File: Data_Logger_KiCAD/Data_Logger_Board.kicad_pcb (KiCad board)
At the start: 6 copper layers, 45.1 x 63.7 mm, 98 parts, among them J1 USB_C_Receptacle_USB2.0_16P, J2 Screw_Terminal_01x02, J3 Micro_SD_Card, Q1 Q_NMOS_GSD, SW1 SW_Push, SW2 SW_Push, U1 LSM6DSO32TR, U10 BMP390L, U11 MMC5983MA, U12 AMS1117-3.3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

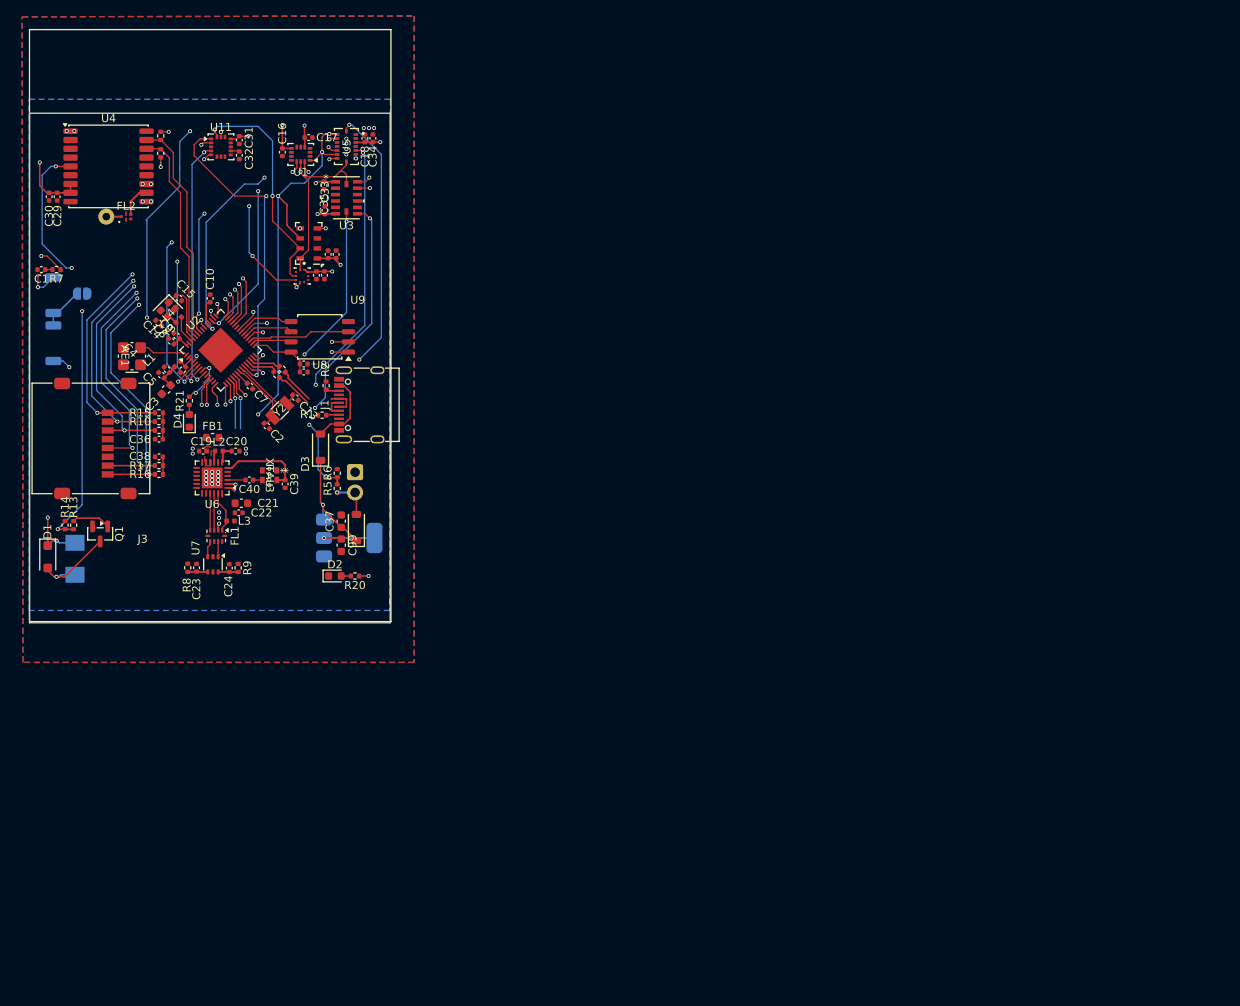
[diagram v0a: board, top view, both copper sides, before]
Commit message: Updates to board routing
Added SMA connector for radio, added additional SPI routing. Reworked some routing for other modules.
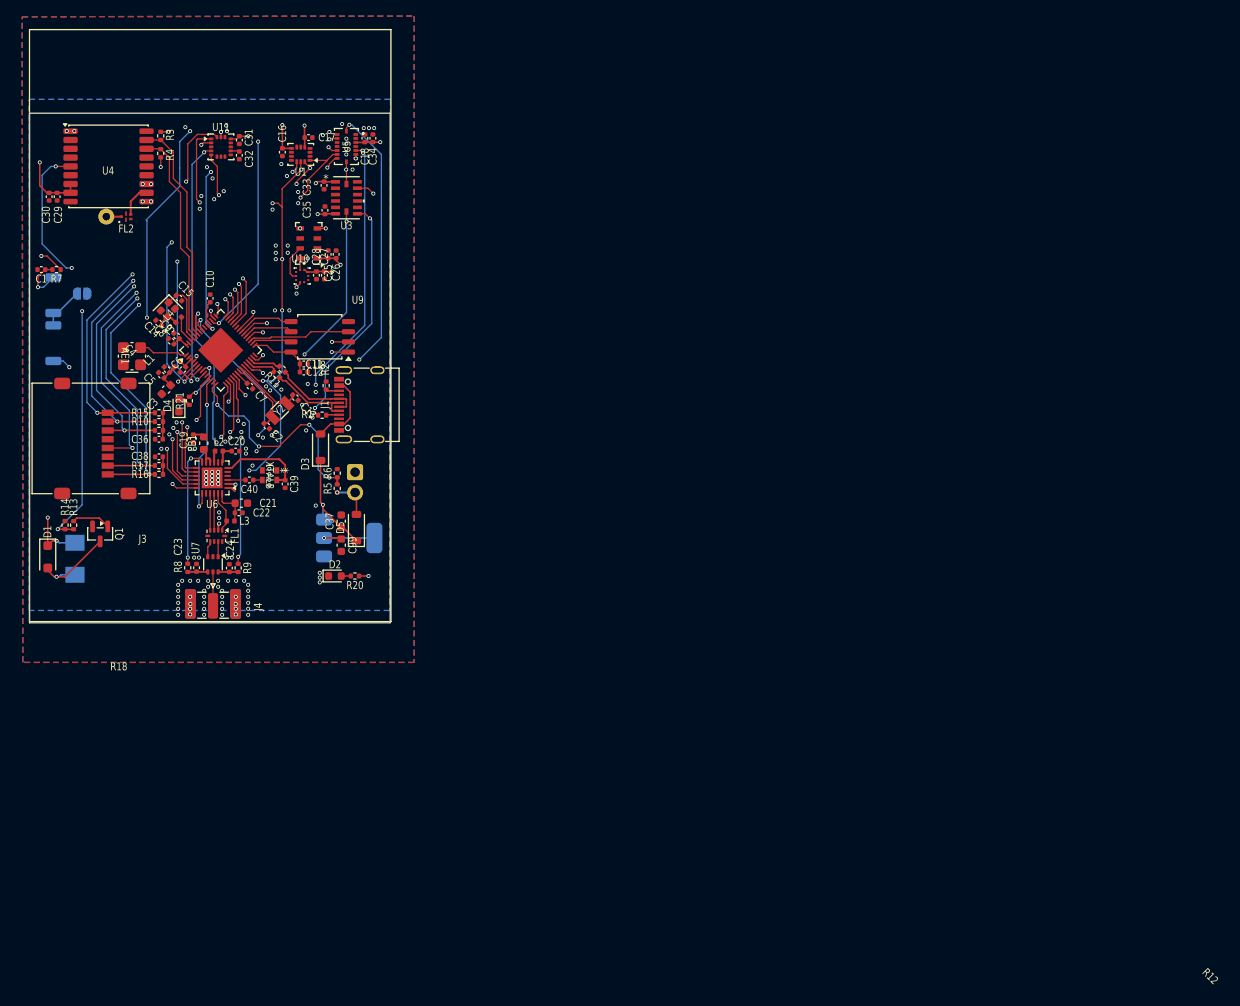
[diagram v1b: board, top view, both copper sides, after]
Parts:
- added J4: Conn_Coaxial_Small, Connector_Coaxial:SMA_Samtec_SMA-J-P-H-ST-EM1_EdgeMount, F.Cu at (142.9, 108.1)
- moved D4 2.30 mm to (138.6, 83.1)
- moved C19 2.00 mm to (140.4, 87.2), turned to -90 degrees
- moved FB1 1.31 mm to (141.7, 87.8), turned to 90 degrees
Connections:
- U7 pad 5: /MCU/radio/SMA_CONN -> /MCU/SMA_CONN
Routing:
- net /MCU/MISO: track 108.9 -> 57.8 mm, vias 9 -> 5
- net /MCU/ANT_SW: track 0.00 -> 37.7 mm, vias 0 -> 4
- net /MCU/SCK: track 69.2 -> 96.8 mm, vias 3 -> 10
- net /MCU/MOSI: track 78.5 -> 54.8 mm
- net /MCU/radio/DIO2: track 0.00 -> 15.2 mm, vias 0 -> 2
- net /MCU/~{RADIO_CS}: track 3.37 -> 18.3 mm, vias 1 -> 2
- net /MCU/~{RADIO_RESET}: track 6.34 -> 21.1 mm, vias 1 -> 2
- net /MCU/RADIO_INT: track 6.82 -> 19.0 mm, vias 1 -> 2
- net /MCU/RADIO_BUSY: track 3.80 -> 15.8 mm, vias 1 -> 2
- net /MCU/MAG_INT: track 39.2 -> 31.6 mm, vias 4 -> 3
- net Net-(U6-VR_PA): track 0.61 -> 5.61 mm
- net /MCU/SMA_CONN: track 0.00 -> 4.25 mm
- net /MCU/BATTERY_SENSE: track 25.3 -> 28.7 mm, vias 3 -> 4
- net /MCU/~{IMU_CS}: track 29.5 -> 32.9 mm
- net /MCU/USB_D-: track 8.55 -> 11.5 mm
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- removed copper zone on F.Cu, net +3V3

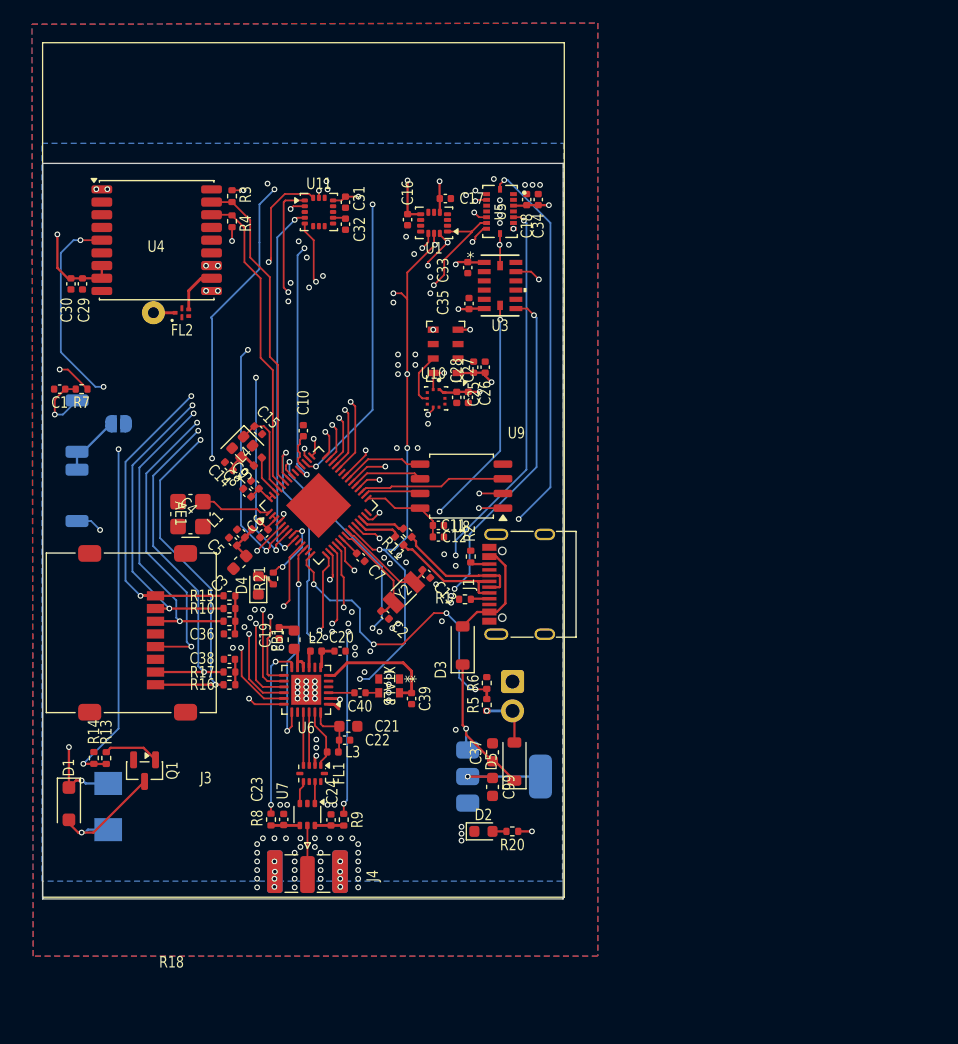
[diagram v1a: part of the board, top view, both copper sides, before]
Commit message: layout
fix rf, usb netclass, add timepulse, round dimensions to even number, re-route GPS, 22 ohm in usb line, buttons to front, reg to front, change solder jumper for conn
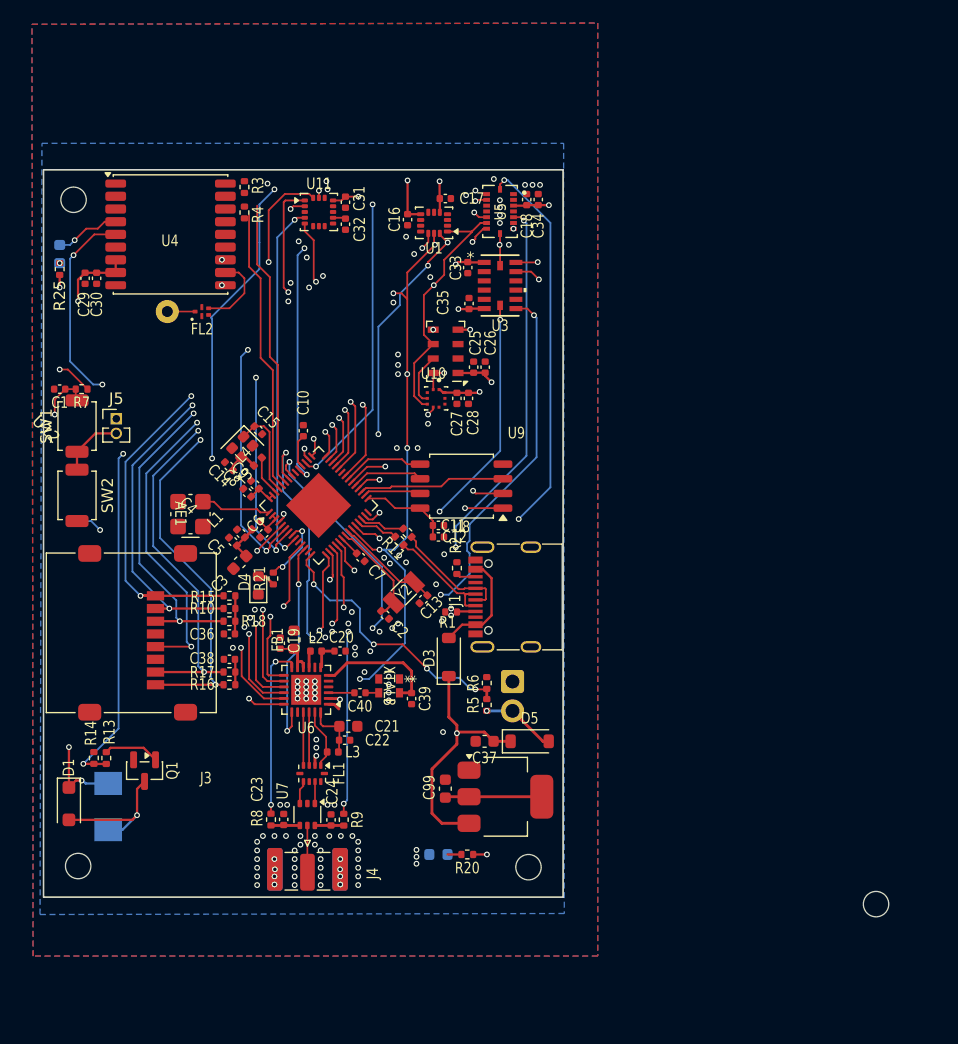
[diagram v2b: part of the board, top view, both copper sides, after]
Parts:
- removed JP1: SolderJumper_2_Open, Jumper:SolderJumper-2_P1.3mm_Open_RoundedPad1.0x1.5mm
- added D6: LED, LED_SMD:LED_0603_1608Metric, B.Cu at (121.4, 54.4)
- added J5: Conn_01x02, Connector_PinHeader_1.27mm:PinHeader_1x02_P1.27mm_Vertical, F.Cu at (126.3, 68.7)
- added R25: 49.9, Resistor_SMD:R_0402_1005Metric, F.Cu at (121.4, 55.7)
- added REF**: MountingHole_2.2mm_M2, MountingHole:MountingHole_2.2mm_M2, F.Cu at (123.0, 107.4)
- added REF**: MountingHole_2.2mm_M2, MountingHole:MountingHole_2.2mm_M2, F.Cu at (162.0, 107.5)
- added REF**: MountingHole_2.2mm_M2, MountingHole:MountingHole_2.2mm_M2, F.Cu at (122.6, 49.7)
- added REF**: MountingHole_2.2mm_M2, MountingHole:MountingHole_2.2mm_M2, F.Cu at (192.1, 110.7)
- D2: moved to B.Cu
- R11, R12: value 0 -> 22
- SW1, SW2, U12: moved to F.Cu
- moved D2 4.38 mm to (154.2, 106.4)
- moved R20 4.38 mm to (156.7, 106.4)
- moved C99 4.09 mm to (154.8, 100.7), turned to 90 degrees
- moved C30 2.28 mm to (124.6, 56.5)
- moved C13 2.21 mm to (152.9, 84.3), turned to -135 degrees
- moved D5 2.19 mm to (162.1, 96.6), turned to 0 degrees
- moved U12 1.75 mm to (160.0, 101.4)
- moved FL2 1.73 mm to (133.7, 59.4)
- moved J1 1.63 mm to (161.1, 84.1)
- moved R1 1.63 mm to (155.3, 85.4)
- moved D3 1.56 mm to (155.1, 89.3)
- moved R2 1.56 mm to (155.8, 81.6)
- moved R3 1.33 mm to (137.4, 48.6)
- moved R4 1.32 mm to (137.4, 50.8)
- moved U4 1.30 mm to (131.0, 52.7)
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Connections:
- C19 pad 1: +3V3 -> Net-(U6-VBAT)
- U2 pad 13: unconnected-(U2-GPIO8-Pad13) -> /MCU/TIMEPULSE
- U4 pad 4: unconnected-(U4-TIMEPULSE-Pad4) -> /MCU/TIMEPULSE
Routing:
- net /MCU/MOSI: track 54.8 -> 105.9 mm, vias 7 -> 9
- net /MCU/MISO: track 57.8 -> 70.2 mm
- net /MCU/PWR_IN: track 13.9 -> 21.7 mm
- net /MCU/TIMEPULSE: track 0.00 -> 5.83 mm, vias 0 -> 1
- net /MCU/BATTERY_SENSE: track 28.7 -> 23.9 mm
- net +3V3: track 76.0 -> 71.7 mm, vias 18 -> 16
- net /MCU/SCL: track 28.0 -> 25.0 mm
- net Net-(FL2-OUT): track 4.05 -> 6.80 mm
- net /MCU/SDA: track 27.0 -> 24.6 mm
- net +BATT: track 5.04 -> 6.46 mm
- net /MCU/~{RESET}: track 33.5 -> 32.1 mm
- net Net-(U6-VBAT): track 4.06 -> 5.27 mm
- net Net-(BZ1--): track 11.4 -> 12.3 mm
- net /MCU/USB_D-: track 11.5 -> 10.7 mm
- net /MCU/USB_D+: track 11.2 -> 10.4 mm
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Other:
- board size 45.1 x 63.7 mm -> 45 x 63 mm

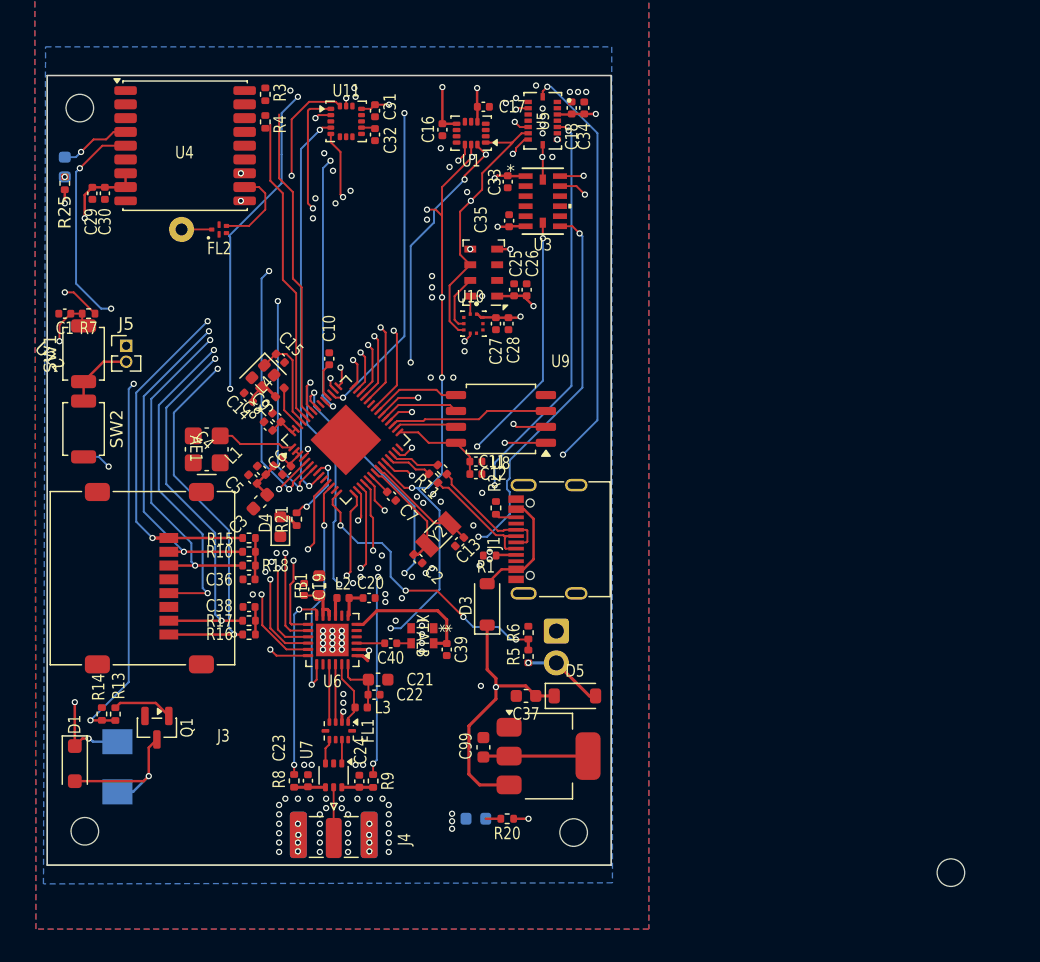
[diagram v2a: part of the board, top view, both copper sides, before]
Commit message: round corners, place mounting holes
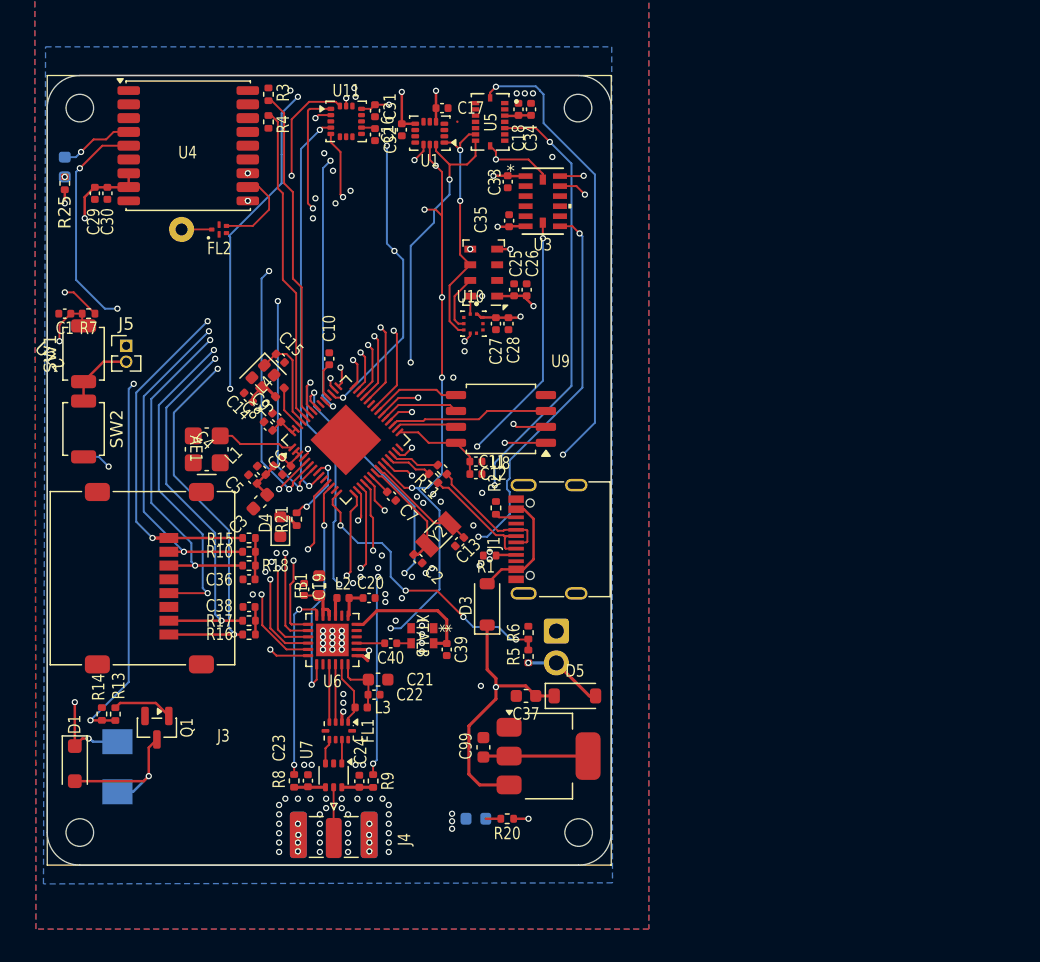
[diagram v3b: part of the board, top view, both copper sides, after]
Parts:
- moved REF** 67.8 mm to (162.4, 49.7)
- moved C18 4.25 mm to (157.6, 49.8)
- moved C34 4.25 mm to (158.6, 49.8)
- moved U5 4.20 mm to (155.3, 50.8)
- moved U1 3.30 mm to (150.5, 51.7)
- moved C17 3.30 mm to (151.5, 49.7)
- moved C16 3.24 mm to (148.3, 51.4)
- moved REF** 0.41 mm to (122.6, 107.5)
- moved REF** 0.40 mm to (162.4, 107.5)
- moved R3 0.25 mm to (137.7, 48.6)
- moved R4 0.25 mm to (137.7, 50.8)
- moved U4 0.25 mm to (131.2, 52.7)
- moved C29 0.20 mm to (123.8, 56.5)
- moved C30 0.20 mm to (124.8, 56.5)
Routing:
- net /MCU/ACCEL_INT: track 48.7 -> 52.1 mm
- net /MCU/~{IMU_CS}: track 32.9 -> 29.5 mm
- net /MCU/~{GYRO_CS}: track 45.0 -> 47.8 mm
- net +3V3: track 71.7 -> 69.2 mm, vias 16 -> 14
- net /MCU/MISO: track 70.2 -> 67.7 mm, vias 5 -> 6
- net /MCU/SCL: track 25.0 -> 26.6 mm
- net /MCU/SCK: track 96.8 -> 98.3 mm
- net /MCU/MOSI: track 105.9 -> 104.5 mm, vias 9 -> 7
- net /MCU/GPS_EXTINT: track 47.3 -> 48.2 mm
- net /MCU/SDA: track 24.6 -> 25.5 mm
- net GND: vias 125 -> 109
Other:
- outline, holes or cut-outs redrawn
